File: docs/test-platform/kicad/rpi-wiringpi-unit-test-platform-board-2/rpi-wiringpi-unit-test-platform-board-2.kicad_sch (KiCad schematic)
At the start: 18 parts, among them J1 IN_PWR_SERVO, J2 IN_I2C_SPI, J3 IN_CS_SR, J4 Servo, M1 ADS1115_0x48, SW1 SW_DIP_x01, U1 74HC595, U2 MCP3008, U3 MCP4922, U4 MCP42010

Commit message: Updated boards
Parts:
- removed J1: IN_PWR_SERVO, rpi-wiringpi-unit-test-platform-board-2:J1, symbol rpi-wiringpi-unit-test-platform-board-2:J1
- removed J2: IN_I2C_SPI, rpi-wiringpi-unit-test-platform-board-2:J2, symbol rpi-wiringpi-unit-test-platform-board-2:J2
- removed J4: Servo, rpi-wiringpi-unit-test-platform-board-2:J4, symbol rpi-wiringpi-unit-test-platform-board-2:J4
- removed M1: ADS1115_0x48, rpi-wiringpi-unit-test-platform-board-2:M1, symbol rpi-wiringpi-unit-test-platform-board-2:M1
- removed U1: 74HC595, rpi-wiringpi-unit-test-platform-board-2:U1, symbol rpi-wiringpi-unit-test-platform-board-2:U1
- removed U2: MCP3008, rpi-wiringpi-unit-test-platform-board-2:U2, symbol rpi-wiringpi-unit-test-platform-board-2:U2
- removed U3: MCP4922, rpi-wiringpi-unit-test-platform-board-2:U3, symbol rpi-wiringpi-unit-test-platform-board-2:U3
- removed U4: MCP42010, rpi-wiringpi-unit-test-platform-board-2:U4, symbol rpi-wiringpi-unit-test-platform-board-2:U4
- added C7: 470µF, Capacitor_THT:CP_Radial_D6.3mm_P2.50mm, symbol Device:C
- added J1: IN_PWR, Connector_JST:JST_XH_B4B-XH-A_1x04_P2.50mm_Vertical, symbol Connector:Conn_01x04_Pin
- added J2: IN_SIGNAL, Connector_JST:JST_XH_B6B-XH-A_1x06_P2.50mm_Vertical, symbol Connector:Conn_01x06_Pin
- added J5: OUT_SERVO, Connector_JST:JST_XH_B3B-XH-A_1x03_P2.50mm_Vertical, symbol Connector:Conn_01x03_Pin
- added U1: MCP3008, Package_DIP:DIP-16_W7.62mm, symbol Analog_ADC:MCP3008
- added U2: MCP4922, Package_DIP:DIP-14_W7.62mm, symbol Analog_DAC:MCP4922
- added U3: MCP42010, Package_DIP:DIP-14_W7.62mm, symbol Potentiometer_Digital:MCP42010
- added U4: ADS1115, RPi:ADS1115_Breakout, symbol RPi:ADS1115_ADC
- added U5: 74HC595, Package_DIP:DIP-16_W7.62mm, symbol 74xx:74HC595
- C6: footprint Capacitor_THT:C_Disc_D3.0mm_W2.0mm_P2.50mm -> Capacitor_THT:CP_Radial_D6.3mm_P2.50mm
- J3: value IN_CS_SR -> IN_CS_SHIFTREG; footprint rpi-wiringpi-unit-test-platform-board-2:J3 -> Connector_JST:JST_XH_B6B-XH-A_1x06_P2.50mm_Vertical
- SW1: value SW_DIP_x01 -> SW_BOARD_CONN_LED
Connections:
- net +3V3: now also J1.2 (Pin_2), J1.4 (Pin_4), U1.15 (Vref), U1.16 (Vdd), U2.1 (Vdd), U2.11 (VrefB), U2.13 (VrefA), U2.9 (~{SHDN}), U3.11 (~{RS}), U3.12 (~{SHDN}), U3.14 (VDD), U3.7 (PA1), U3.8 (PA0), U4.1 (VDD), U5.10 (~{SRCLR}), U5.16 (VCC); no longer C6.1
- net +5V: now also C6.1, C7.1, J1.1 (Pin_1), J5.3 (Pin_3)
- net CS_ADC: now also U1.10 (~{CS}/SHDN)
- net CS_DAC: now also U2.3 (~{CS})
- net CS_DPOT: now also U3.1 (~{CS})
- net DAC_A_CH1: now also U1.2 (CH1), U2.14 (VA)
- net DAC_B_CH3: now also U1.4 (CH3), U2.10 (VB)
- net GND: now also C7.2, J1.3 (Pin_3), J5.2 (Pin_2), U1.14 (AGND), U1.9 (DGND), U2.12 (Vss), U2.8 (~{LDAC}), U3.10 (PB0), U3.4 (VSS), U3.5 (PB1), U4.2 (GND), U4.5 (ADDR), U5.13 (~{OE}), U5.8 (GND)
- net I2C_SCL: now also J2.2 (Pin_2), U4.3 (SCL)
- net I2C_SDA: now also J2.1 (Pin_1), U4.4 (SDA)
- net PWM18: now also J2.6 (Pin_6), J5.1 (Pin_1), U4.7 (A0)
- net SPI_MISO: now also J2.3 (Pin_3), U1.12 (Dout)
- net SPI_MOSI: now also J2.4 (Pin_4), U1.11 (Din), U2.5 (SDI), U3.3 (SI)
- net SPI_SCLK: now also J2.5 (Pin_5), U1.13 (CLK), U2.4 (SCK), U3.2 (SCK)
- net SR_CLK: now also U5.11 (SRCLK)
- net SR_DATA: now also U5.14 (SER)
- net SR_LATCH: now also U5.12 (RCLK)
- net SR_Q_CH2: now also U1.3 (CH2), U5.1 (QB)
- new net DPOT_WIPER_A: U3.9 (PW0), U4.8 (A1)
- new net DPOT_WIPER_B: U3.6 (PW1), U4.9 (A2)
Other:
- moved on the sheet: C2, C3, C4, C5, C6, D1, J3, R1, SW1

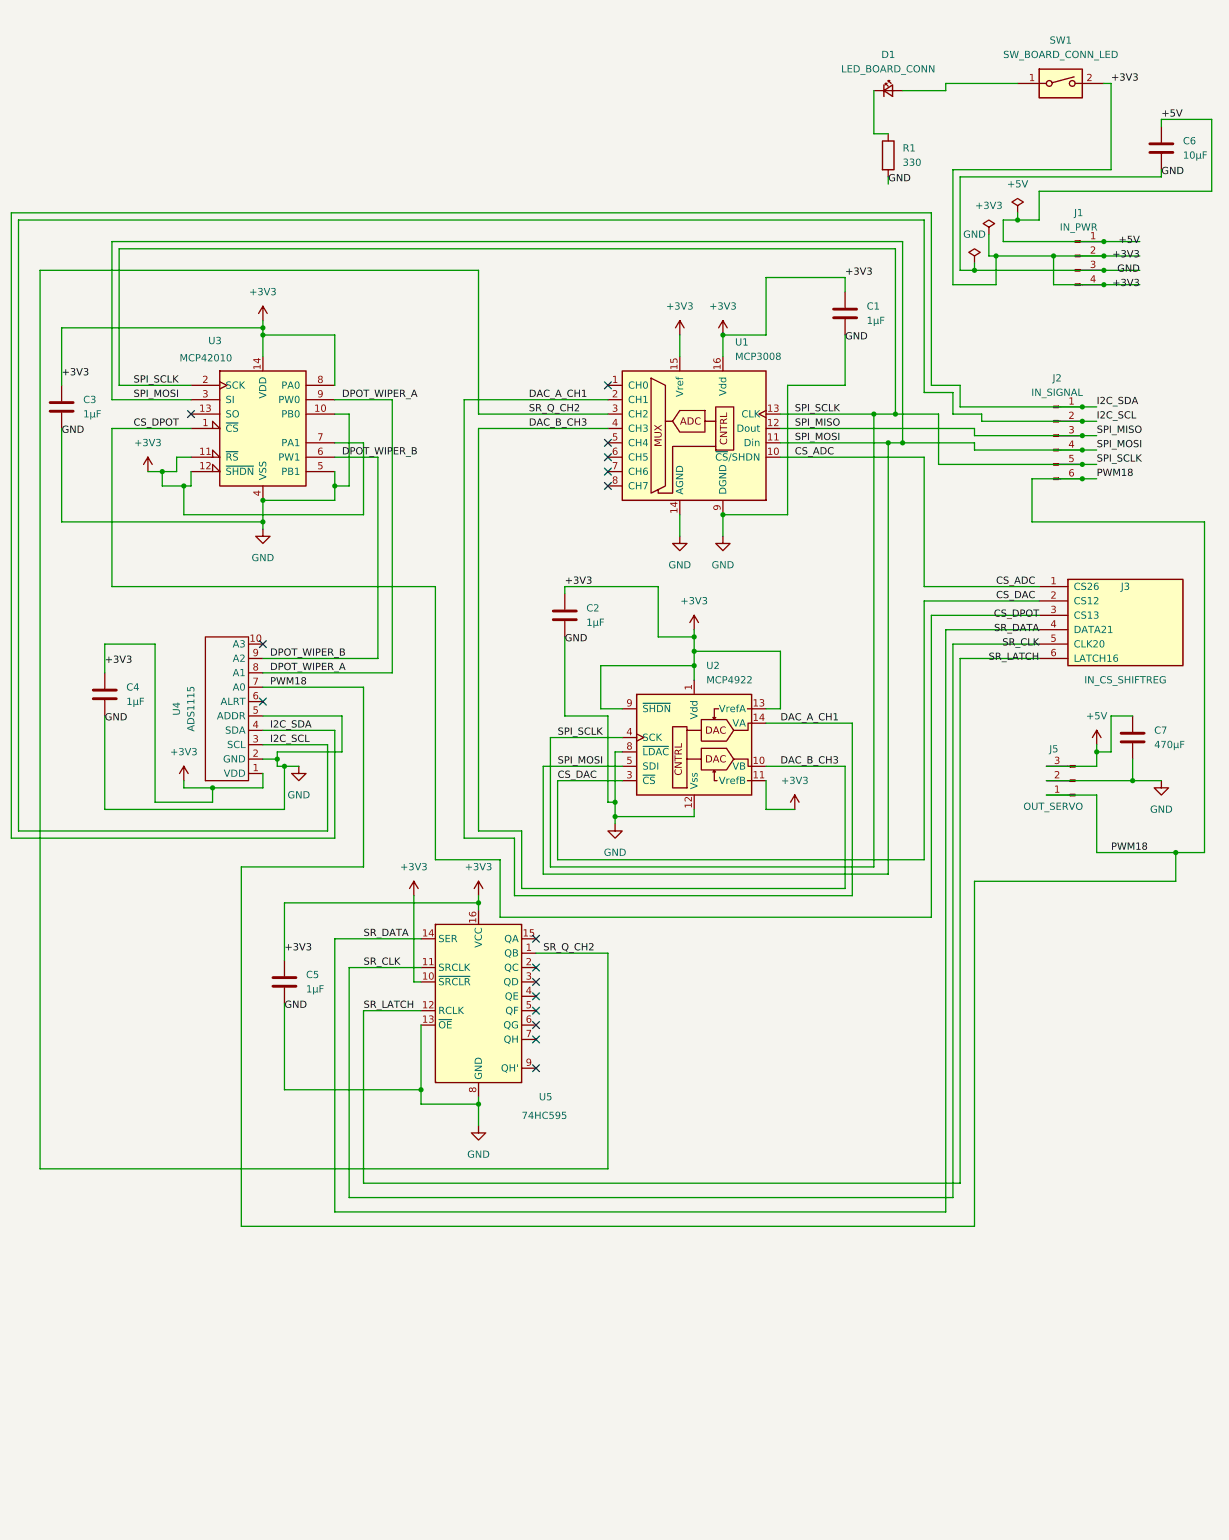
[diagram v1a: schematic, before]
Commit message: Add proper caps; clean up tracing, update mislabeled caps
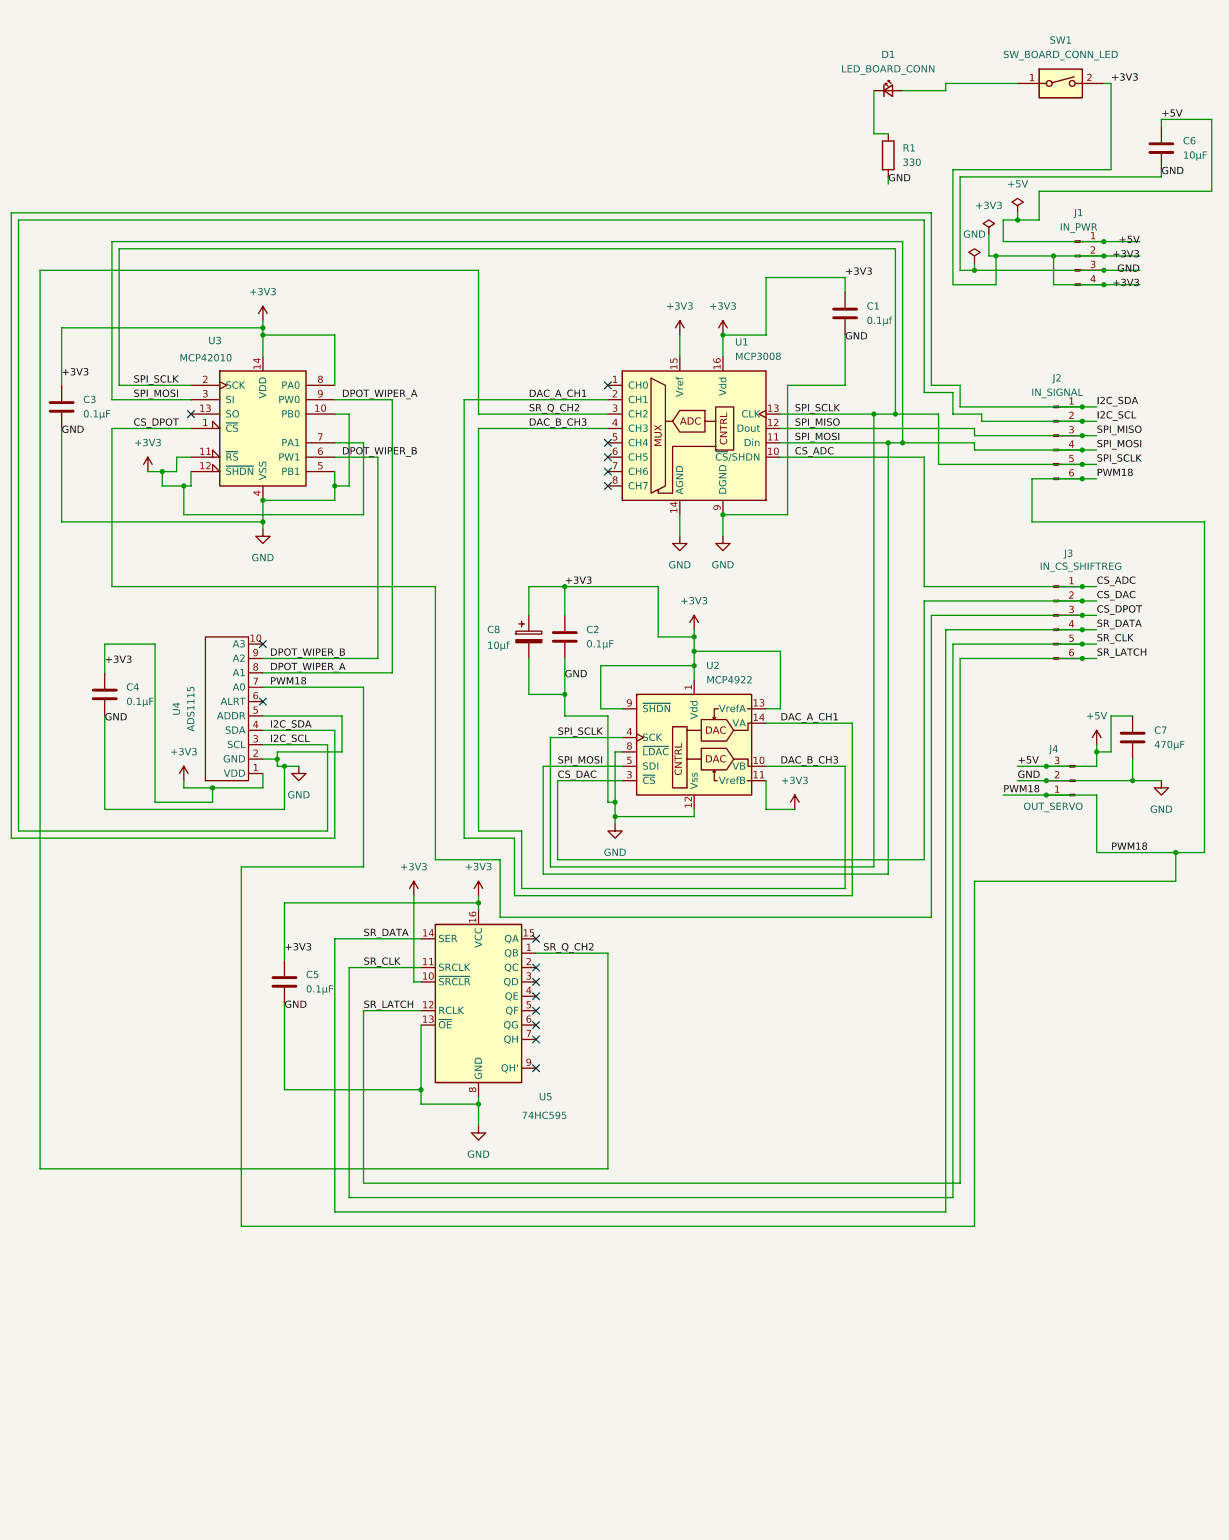
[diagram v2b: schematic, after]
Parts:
- removed J3: IN_CS_SHIFTREG, Connector_JST:JST_XH_B6B-XH-A_1x06_P2.50mm_Vertical, symbol rpi-wiringpi-unit-test-platform-board-2:J3
- added C8: 10µf, Capacitor_THT:CP_Radial_D5.0mm_P2.50mm, symbol Device:C_Polarized
- added J3: IN_CS_SHIFTREG, Connector_JST:JST_XH_B6B-XH-A_1x06_P2.50mm_Vertical, symbol Connector:Conn_01x06_Pin
- C1: value 1µF -> 0.1µf
- C2, C3, C4, C5: value 1µF -> 0.1µF
- renumbered J5 to J4
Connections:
- net +3V3: now also C8.1
- net CS_ADC: now also J3.1 (Pin_1)
- net CS_DAC: now also J3.2 (Pin_2)
- net CS_DPOT: now also J3.3 (Pin_3)
- net GND: now also C8.2
- net SR_CLK: now also J3.5 (Pin_5)
- net SR_DATA: now also J3.4 (Pin_4)
- net SR_LATCH: now also J3.6 (Pin_6)
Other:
- moved on the sheet: C2

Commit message: Added JST for future servo position sensors (connected to MCP3008)
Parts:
- added J5: OUT_SERVO_SIG, Connector_JST:JST_XH_B3B-XH-A_1x03_P2.50mm_Vertical, symbol Connector:Conn_01x03_Pin
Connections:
- net +3V3: now also J5.1 (Pin_1)
- net CCW: now reaches U1.7 (CH6)
- net CCW: now also J5.2 (Pin_2)
- net CW: now reaches U1.8 (CH7)
- net CW: now also J5.3 (Pin_3)
- no-connect marks 16 -> 14
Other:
- moved on the sheet: D1

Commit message: Tweaks and cleanup
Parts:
- added C9: 0.1µf, Capacitor_THT:C_Disc_D3.0mm_W2.0mm_P2.50mm, symbol Device:C
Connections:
- net +5V: now also C9.1
- net GND: now also C9.2
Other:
- moved on the sheet: C7
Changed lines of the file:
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@@
 	)
 	(junction
-		(at 212.09 157.48)
-		(diameter 0)
-		(color 0 0 0 0)
-	)
-	(junction
 		(at 49.53 158.75)
 		(diameter 0)
@@
 	)
 	(junction
+		(at 212.09 146.05)
+		(diameter 0)
+		(color 0 0 0 0)
+	)
+	(junction
 		(at 196.85 157.48)
 		(diameter 0)
@@
 	)
 	(junction
+		(at 217.17 157.48)
+		(diameter 0)
+		(color 0 0 0 0)
+	)
+	(junction
+		(at 212.09 157.48)
+		(diameter 0)
+		(color 0 0 0 0)
+	)
+	(junction
 		(at 191.77 58.42)
 		(diameter 0)
@@
 	(wire
 		(pts
+			(xy 212.09 153.67) (xy 212.09 157.48)
+		)
+		(stroke
+			(width 0)
+			(type default)
+		)
+	)
+	(wire
+		(pts
 			(xy 147.32 157.48) (xy 147.32 162.56)
 		)
@@
 	(wire
 		(pts
-			(xy 212.09 157.48) (xy 217.17 157.48)
-		)
-		(stroke
-			(width 0)
-			(type default)
-		)
-	)
-	(wire
-		(pts
 			(xy 58.42 138.43) (xy 81.28 138.43)
 		)
@@
 	(wire
 		(pts
+			(xy 212.09 157.48) (xy 217.17 157.48)
+		)
+		(stroke
+			(width 0)
+			(type default)
+		)
+	)
+	(wire
+		(pts
 			(xy 110.49 157.48) (xy 121.92 157.48)
 		)
@@
 	(wire
 		(pts
+			(xy 220.98 157.48) (xy 217.17 157.48)
+		)
+		(stroke
+			(width 0)
+			(type default)
+		)
+	)
+	(wire
+		(pts
 			(xy 198.12 69.85) (xy 207.01 69.85)
 		)
@@
 	(wire
 		(pts
+			(xy 217.17 160.02) (xy 217.17 157.48)
+		)
+		(stroke
+			(width 0)
+			(type default)
+		)
+	)
+	(wire
+		(pts
 			(xy 69.85 151.13) (xy 69.85 166.37)
 		)
@@
 	(wire
 		(pts
+			(xy 212.09 146.05) (xy 220.98 146.05)
+		)
+		(stroke
+			(width 0)
+			(type default)
+		)
+	)
+	(wire
+		(pts
 			(xy 105.41 104.14) (xy 105.41 107.95)
 		)
@@
 	(wire
 		(pts
-			(xy 212.09 153.67) (xy 212.09 157.48)
+			(xy 220.98 153.67) (xy 220.98 157.48)
 		)
 		(stroke
@@
 	(symbol
 		(lib_id "Device:C")
-		(at 212.09 149.86 0)
+		(at 220.98 149.86 0)
 		(unit 1)
 		(body_style 1)
@@
 		(in_pos_files yes)
 		(dnp no)
-		(fields_autoplaced yes)
 		(property "Reference" "C7"
-			(at 215.9 148.5899 0)
+			(at 217.932 142.24 0)
 			(show_name no)
 			(do_not_autoplace no)
@@
 		)
 		(property "Value" "470µF"
-			(at 215.9 151.1299 0)
+			(at 217.932 144.78 0)
 			(show_name no)
 			(do_not_autoplace no)
@@
 		)
 		(property "Footprint" "Capacitor_THT:CP_Radial_D6.3mm_P2.50mm"
-			(at 213.36 153.67 0)
+			(at 222.25 153.67 0)
 			(hide yes)
 			(show_name no)
@@
 		)
 		(property "Datasheet" ""
-			(at 212.09 149.86 0)
+			(at 220.98 149.86 0)
 			(hide yes)
 			(show_name no)
@@
 		)
 		(property "Description" "Unpolarized capacitor"
-			(at 212.09 149.86 0)
+			(at 220.98 149.86 0)
 			(hide yes)
 			(show_name no)
@@
 	(symbol
 		(lib_id "power:GND")
-		(at 217.17 157.48 0)
+		(at 217.17 160.02 0)
 		(unit 1)
 		(body_style 1)
@@
 		(fields_autoplaced yes)
 		(property "Reference" "#PWR016"
-			(at 217.17 163.83 0)
+			(at 217.17 166.37 0)
 			(hide yes)
 			(show_name no)
@@
 		)
 		(property "Value" "GND"
-			(at 217.17 162.56 0)
+			(at 217.17 165.1 0)
 			(show_name no)
 			(do_not_autoplace no)
@@
 		)
 		(property "Footprint" ""
-			(at 217.17 157.48 0)
+			(at 217.17 160.02 0)
 			(hide yes)
 			(show_name no)
@@
 		)
 		(property "Datasheet" ""
-			(at 217.17 157.48 0)
+			(at 217.17 160.02 0)
 			(hide yes)
 			(show_name no)
@@
 		)
 		(property "Description" "Power symbol creates a global label with name \"GND\" , ground"
-			(at 217.17 157.48 0)
+			(at 217.17 160.02 0)
 			(hide yes)
 			(show_name no)
@@
 					(unit 1)
 				)
+			)
+		)
+	)
+	(symbol
+		(lib_id "Device:C")
+		(at 212.09 149.86 0)
+		(unit 1)
+		(body_style 1)
+		(exclude_from_sim no)
+		(in_bom yes)
+		(on_board yes)
+		(in_pos_files yes)
+		(dnp no)
+		(property "Reference" "C9"
+			(at 210.566 141.986 0)
+			(show_name no)
+			(do_not_autoplace no)
+			(effects
+				(font
+					(size 1.27 1.27)
+				)
+				(justify left)
+			)
+		)
+		(property "Value" "0.1µf"
+			(at 210.566 144.526 0)
+			(show_name no)
+			(do_not_autoplace no)
+			(effects
+				(font
+					(size 1.27 1.27)
+				)
+				(justify left)
+			)
+		)
+		(property "Footprint" "Capacitor_THT:C_Disc_D3.0mm_W2.0mm_P2.50mm"
+			(at 213.36 153.67 0)
+			(hide yes)
+			(show_name no)
+			(do_not_autoplace no)
+			(effects
+				(font
+					(size 1.27 1.27)
+				)
+			)
+		)
+		(property "Datasheet" ""
+			(at 212.09 149.86 0)
+			(hide yes)
+			(show_name no)
+			(do_not_autoplace no)
+			(effects
+				(font
+					(size 1.27 1.27)
+				)
+			)
+		)
+		(property "Description" "Unpolarized capacitor"
+			(at 212.09 149.86 0)
+			(hide yes)
+			(show_name no)
+			(do_not_autoplace no)
+			(effects
+				(font
+					(size 1.27 1.27)
+				)
+			)
+		)
+		(pin "1"
+		)
+		(pin "2"
+		)
+		(instances
+			(project "rpi-wiringpi-unit-test-platform-board-2"
+				(path "/7946ceed-5e50-51f0-9396-19e4533fa9f5"
+					(reference "C9")
+					(unit 1)
+				)
